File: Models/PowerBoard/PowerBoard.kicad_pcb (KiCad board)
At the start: 2 copper layers, 44 parts, among them J11 Conn_01x09_Socket, J12 Banana Socket, Green, J13 Banana Socket, Black, J14 Banana Socket, Blue, U1 LM7815, 15V, 5%, U2 LM7805, 5V, 5%, U3 LM7915, -15V, 5%, U4 TLV76133, 3.3V, 1%, U5 LM7805, 5V, 5%, U6 LM7905, -5V, 5%

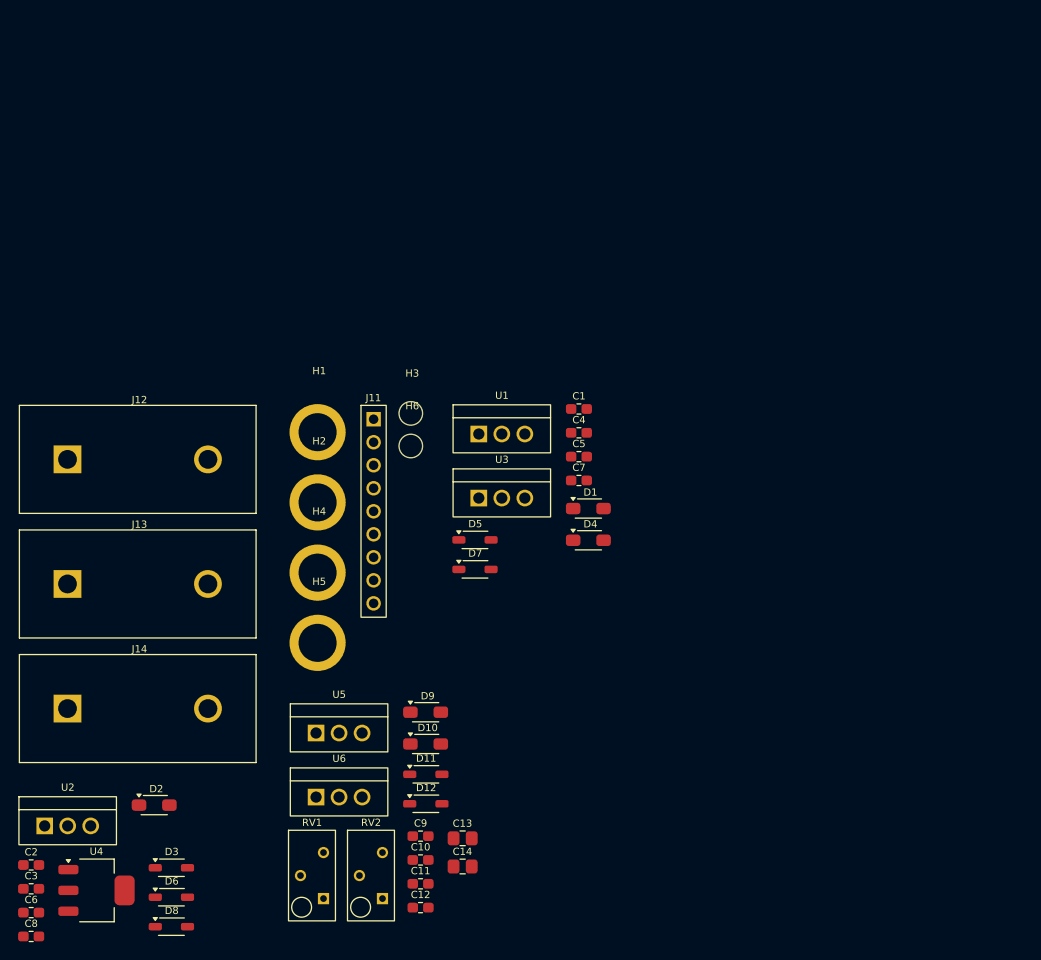
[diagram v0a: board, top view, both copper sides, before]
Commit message: Everything is now aligned very well on the power board
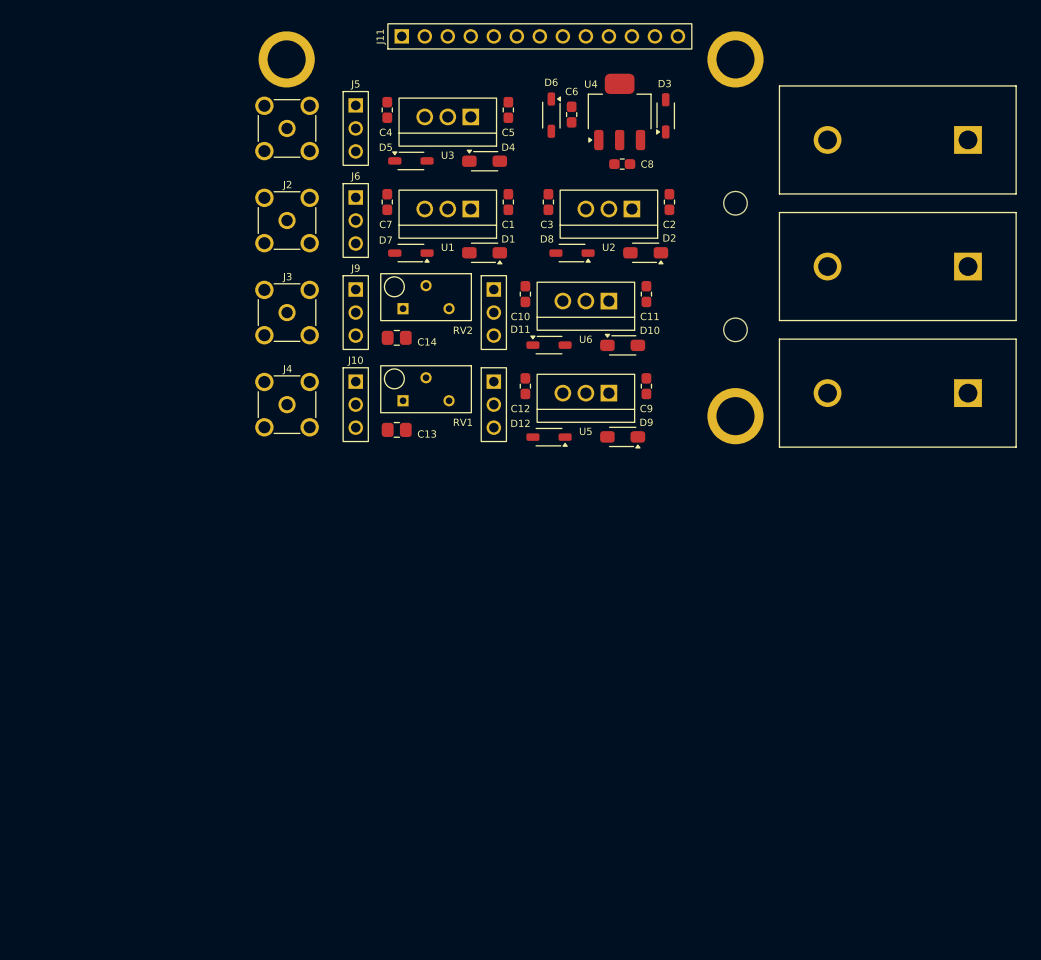
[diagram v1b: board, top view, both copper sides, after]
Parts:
- removed H6: Dowel Pin, M2.5, Connector_Custom:DowelPin_2.5mm
- added J1: Conn_Coaxial, Connector_Custom:Molex_MCX, F.Cu at (130.4, 43.3)
- added J10: Conn_01x03_Pin, Connector_Custom:PinConnector_1x3, F.Cu at (138.0, 73.7)
- added J2: Conn_Coaxial, Connector_Custom:Molex_MCX, F.Cu at (130.4, 53.4)
- added J3: Conn_Coaxial, Connector_Custom:Molex_MCX, F.Cu at (130.4, 63.6)
- added J4: Conn_Coaxial, Connector_Custom:Molex_MCX, F.Cu at (130.4, 73.7)
- added J5: Conn_01x03_Pin, Connector_Custom:PinConnector_1x3, F.Cu at (138.0, 43.3)
- added J6: Conn_01x03_Pin, Connector_Custom:PinConnector_1x3, F.Cu at (138.0, 53.4)
- added J7: Conn_01x03_Pin, Connector_Custom:PinConnector_1x3, F.Cu at (153.2, 63.6)
- added J8: Conn_01x03_Pin, Connector_Custom:PinConnector_1x3, F.Cu at (153.2, 73.7)
- added J9: Conn_01x03_Pin, Connector_Custom:PinConnector_1x3, F.Cu at (138.0, 63.6)
- H5: value Mounting Hole, M2.5 -> Dowel Pin, M2.5; footprint Connector_Custom:Keystone_24929 -> Connector_Custom:DowelPin_2.5mm
- J11: value Conn_01x09_Socket -> Conn_01x13_Socket; footprint Connector_Custom:PinConnector_1x9 -> Connector_Custom:PinConnector_1x13
- moved C8 107.3 mm to (167.4, 47.2), turned to 180 degrees
- moved C6 106.4 mm to (161.8, 41.7), turned to -90 degrees
- moved J14 104.8 mm to (197.8, 44.5), turned to 180 degrees
- moved U4 103.5 mm to (167.1, 41.4), turned to 90 degrees
- moved C2 101.6 mm to (172.6, 51.4), turned to 90 degrees
- moved D3 99.3 mm to (172.2, 41.9), turned to 90 degrees
- moved D6 96.0 mm to (159.6, 41.8), turned to -90 degrees
- moved C3 94.9 mm to (159.3, 51.4), turned to 90 degrees
- moved J13 90.9 mm to (197.8, 58.5), turned to 180 degrees
- moved U2 90.6 mm to (165.9, 52.1), turned to 180 degrees
- moved D8 86.5 mm to (161.9, 57.0), turned to 180 degrees
- moved J12 84.2 mm to (197.8, 72.5), turned to 180 degrees
- moved D2 81.6 mm to (170.0, 57.0), turned to 180 degrees
- moved C11 69.7 mm to (170.1, 61.5), turned to 90 degrees
- moved H2 67.2 mm to (179.9, 35.6)
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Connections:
- J11 pad 2: /15V -> /-15V
- J11 pad 4: /-15V -> /15V
- RV2 pad 1: -5V_PreAmp -> GND
- RV2 pad 3: GND -> -5V_PreAmp

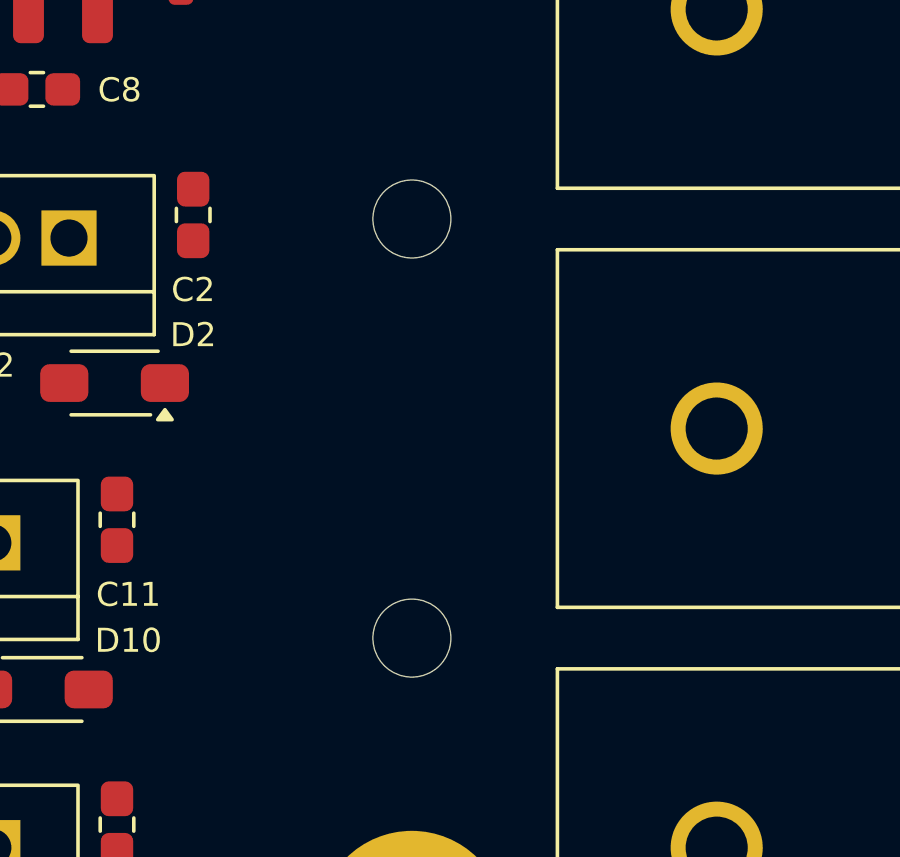
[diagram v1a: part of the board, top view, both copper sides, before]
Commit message: Better dowel pin alignment
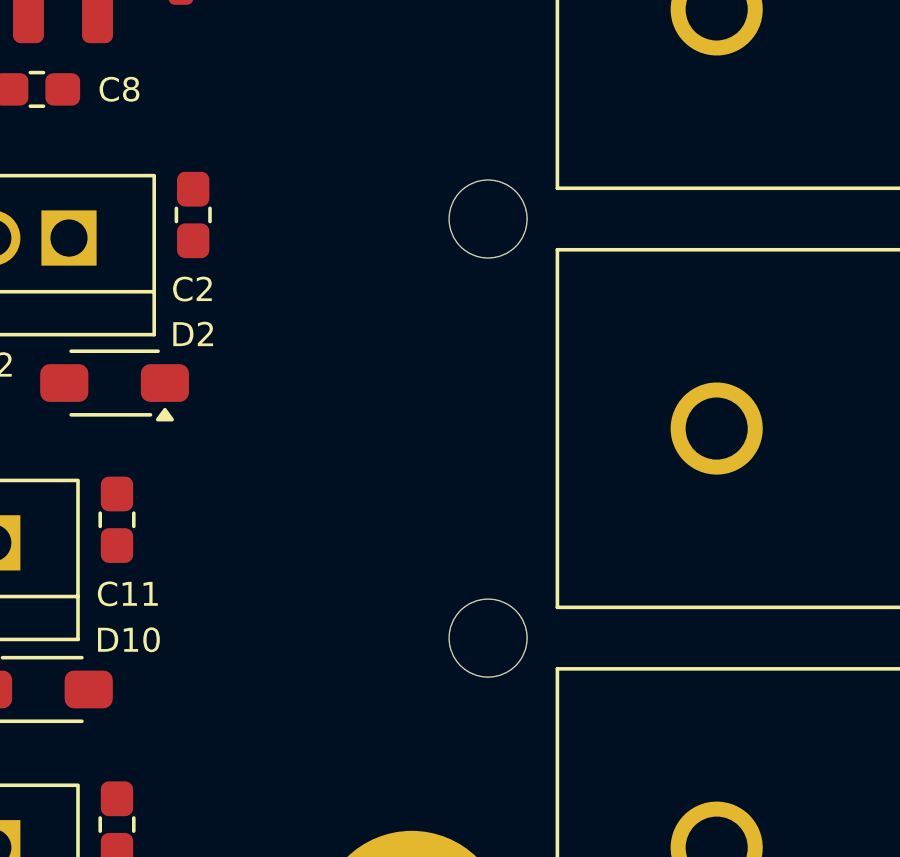
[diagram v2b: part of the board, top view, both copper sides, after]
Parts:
- moved H3 2.54 mm to (182.4, 51.5)
- moved H5 2.54 mm to (182.4, 65.5)
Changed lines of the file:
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@@
 	(footprint "Connector_Custom:DowelPin_2.5mm"
 		(layer "F.Cu")
-		(at 179.91 51.515)
+		(at 182.45 51.515)
 		(property "Reference" "H3"
 			(at 0.16 -4.42 0)
@@
 	(footprint "Connector_Custom:DowelPin_2.5mm"
 		(layer "F.Cu")
-		(at 179.91 65.485)
+		(at 182.45 65.485)
 		(property "Reference" "H5"
 			(at 0.16 -4.42 0)

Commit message: Save progress
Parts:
- J10, J5, J6, J7, J8, J9: footprint Connector_Custom:PinConnector_1x3 -> Connector_Custom:PinHeader_1x3
- J11: footprint Connector_Custom:PinConnector_1x13 -> Connector_Custom:PinSocket_1x13
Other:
- board outline added: 85.8 x 48.2 mm

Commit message: Finished layout of power board
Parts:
- J12: value Banana Socket, Green -> Banana Socket, Red
- J14: value Banana Socket, Blue -> Banana Socket, Yellow
- moved J12 1.80 mm to (196.6, 71.2)
- moved J14 1.80 mm to (196.6, 45.8)
- moved D10 1.27 mm to (167.5, 65.9)
- moved H1 1.27 mm to (131.7, 35.6)
- moved H4 1.27 mm to (179.9, 73.7)
- moved C1 1.27 mm to (154.8, 50.1)
- moved C2 1.27 mm to (172.6, 50.1)
- moved C3 1.27 mm to (159.3, 50.1)
- moved C7 1.27 mm to (141.5, 50.1)
- moved C8 1.27 mm to (167.4, 45.9)
- moved D1 1.27 mm to (152.2, 55.7)
- moved D2 1.27 mm to (170.0, 55.7)
- moved D5 1.27 mm to (144.1, 45.6)
- moved U3 1.27 mm to (148.2, 40.7)
- moved U6 1.27 mm to (163.4, 61.0)
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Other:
- board size 85.8 x 48.2 mm -> 80.8 x 47.1 mm

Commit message: Save progress
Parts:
- moved H5 0.64 mm to (182.4, 64.8)
- moved H3 0.63 mm to (182.4, 52.1)
- moved D3 0.43 mm to (172.2, 40.2)
- moved D6 0.35 mm to (159.6, 40.2)
- moved C6 0.29 mm to (161.8, 40.2)
- moved C8 0.28 mm to (167.1, 45.9)
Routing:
- added copper zone on B.Cu, net GND
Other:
- board size 80.8 x 47.1 mm -> 81.1 x 47.1 mm
- board text added: "-1.5V"
- board text added: "-15V"
- board text added: "-18V"
- board text added: "-5V"
- board text added: "15V"
- board text added: "18V"
- board text added: "2.5V"
- board text added: "3.3V"
- board text added: "5V"
- board text added: "GND"
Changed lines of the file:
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@@
 	(footprint "TwoTerminal:SOD-123"
 		(layer "F.Cu")
-		(at 172.21 40.6 90)
+		(at 172.21 40.17 90)
 		(property "Reference" "D3"
 			(at 3.53 -0.11 0)
@@
 	(footprint "TwoTerminal:CAPC0603"
 		(layer "F.Cu")
-		(at 161.83 40.46 -90)
+		(at 161.83 40.17 -90)
 		(property "Reference" "C6"
 			(at -2.52 -0.01 0)
@@
 	(footprint "TwoTerminal:SOD-123"
 		(layer "F.Cu")
-		(at 159.59 40.52 -90)
+		(at 159.59 40.17 -90)
 		(property "Reference" "D6"
 			(at -3.59 0.01 0)
@@
 	(footprint "TwoTerminal:CAPC0603"
 		(layer "F.Cu")
-		(at 167.41 45.925 180)
+		(at 167.13 45.925 180)
 		(property "Reference" "C8"
 			(at -2.76 -0.025 0)
@@
 	(footprint "Connector_Custom:DowelPin_2.5mm"
 		(layer "F.Cu")
-		(at 182.45 51.515)
+		(at 182.45 52.15)
 		(property "Reference" "H3"
 			(at 0.16 -4.42 0)
@@
 	(footprint "Connector_Custom:DowelPin_2.5mm"
 		(layer "F.Cu")
-		(at 182.45 65.485)
+		(at 182.45 64.85)
 		(property "Reference" "H5"
 			(at 0.16 -4.42 0)
@@
 	(gr_line
 		(start 206.51 78.31)
-		(end 127.745 78.31)
+		(end 127.405 78.31)
 		(stroke
 			(width 0.05)
@@
 	)
 	(gr_arc
-		(start 126.745 32.21)
-		(mid 127.037893 31.502893)
-		(end 127.745 31.21)
+		(start 126.405 32.21)
+		(mid 126.697893 31.502893)
+		(end 127.405 31.21)
 		(stroke
 			(width 0.05)
@@
 	)
 	(gr_arc
-		(start 127.745 78.31)
-		(mid 127.037893 78.017107)
-		(end 126.745 77.31)
+		(start 127.405 78.31)
+		(mid 126.697893 78.017107)
+		(end 126.405 77.31)
 		(stroke
 			(width 0.05)
@@
 	)
 	(gr_line
-		(start 127.745 31.21)
+		(start 127.405 31.21)
 		(end 206.51 31.21)
 		(stroke
@@
 	)
 	(gr_line
-		(start 126.745 77.31)
-		(end 126.745 32.21)
+		(start 126.405 77.31)
+		(end 126.405 32.21)
 		(stroke
 			(width 0.05)
@@
 		(layer "Edge.Cuts")
 	)
+	(gr_text "5V"
+		(at 165.94 54 0)
+		(layer "B.SilkS")
+		(effects
+			(font
+				(size 1.5 1.5)
+				(thickness 0.3)
+				(bold yes)
+			)
+			(justify mirror)
+		)
+	)
+	(gr_text "-15V"
+		(at 148.16 43.84 0)
+		(layer "B.SilkS")
+		(effects
+			(font
+				(size 1.5 1.5)
+				(thickness 0.3)
+				(bold yes)
+			)
+			(justify mirror)
+		)
+	)
+	(gr_text "-5V"
+		(at 163.4 64.16 0)
+		(layer "B.SilkS")
+		(effects
+			(font
+				(size 1.5 1.5)
+				(thickness 0.3)
+				(bold yes)
+			)
+			(justify mirror)
+		)
+	)
+	(gr_text "15V"
+		(at 148.16 54 0)
+		(layer "B.SilkS")
+		(effects
+			(font
+				(size 1.5 1.5)
+				(thickness 0.3)
+				(bold yes)
+			)
+			(justify mirror)
+		)
+	)
+	(gr_text "-1.5V"
+		(at 145.62 65.66 0)
+		(layer "B.SilkS")
+		(effects
+			(font
+				(size 1.5 1.5)
+				(thickness 0.3)
+				(bold yes)
+			)
+			(justify mirror)
+		)
+	)
+	(gr_text "GND"
+		(at 196.55 58.5 0)
+		(layer "B.SilkS")
+		(effects
+			(font
+				(size 1.5 1.5)
+				(thickness 0.3)
+				(bold yes)
+			)
+			(justify mirror)
+		)
+	)
+	(gr_text "3.3V"
+		(at 165.94 43.84 0)
+		(layer "B.SilkS")
+		(effects
+			(font
+				(size 1.5 1.5)
+				(thickness 0.3)
+				(bold yes)
+			)
+			(justify mirror)
+		)
+	)
+	(gr_text "5V"
+		(at 163.4 74.32 0)
+		(layer "B.SilkS")
+		(effects
+			(font
+				(size 1.5 1.5)
+				(thickness 0.3)
+				(bold yes)
+			)
+			(justify mirror)
+		)
+	)
+	(gr_text "2.5V"
+		(at 145.62 75.82 0)
+		(layer "B.SilkS")
+		(effects
+			(font
+				(size 1.5 1.5)
+				(thickness 0.3)
+				(bold yes)
+			)
+			(justify mirror)
+		)
+	)
+	(gr_text "-18V"
+		(at 196.55 45.8 0)
+		(layer "B.SilkS")
+		(effects
+			(font
+				(size 1.5 1.5)
+				(thickness 0.3)
+				(bold yes)
+			)
+			(justify mirror)
+		)
+	)
+	(gr_text "18V"
+		(at 196.55 71.2 0)
+		(layer "B.SilkS")
+		(effects
+			(font
+				(size 1.5 1.5)
+				(thickness 0.3)
+				(bold yes)
+			)
+			(justify mirror)
+		)
+	)
+	(zone
+		(net 1)
+		(net_name "GND")
+		(layer "B.Cu")
+		(hatch edge 0.5)
+		(connect_pads
+			(clearance 0.5)
+		)
+		(min_thickness 0.25)
+		(filled_areas_thickness no)
+		(fill yes
+			(thermal_gap 0.5)
+			(thermal_bridge_width 0.5)
+		)
+		(polygon
+			(pts
+				(xy 126.905 31.71) (xy 126.905 77.81) (xy 207.01 77.81) (xy 207.01 31.71)
+			)
+		)
+	)
 	(embedded_fonts no)

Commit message: First time that all PCBs are fully wired
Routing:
- net /15V/18V: track 0.00 -> 118.7 mm, vias 0 -> 4
- net /15V/-18V: track 0.00 -> 103.8 mm
- net /15V: track 0.00 -> 62.1 mm, vias 0 -> 4
- net /5V: track 0.00 -> 55.1 mm
- net /-15V: track 0.00 -> 41.1 mm
- net GND: track 0.00 -> 29.4 mm, vias 0 -> 19
- net -5V_PreAmp: track 0.00 -> 28.9 mm
- net 5V_PreAmp: track 0.00 -> 28.9 mm
- net /-1.5V: track 0.00 -> 24.5 mm
- net /2.5V: track 0.00 -> 24.5 mm
- net /3.3V: track 0.00 -> 21.1 mm
